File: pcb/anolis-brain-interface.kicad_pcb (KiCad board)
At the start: 2 copper layers, 26 x 26 mm, 12 parts, among them U1 RHD2216, U2 Setebos-I, U3 47571-0001, U4 TPS610994YFF

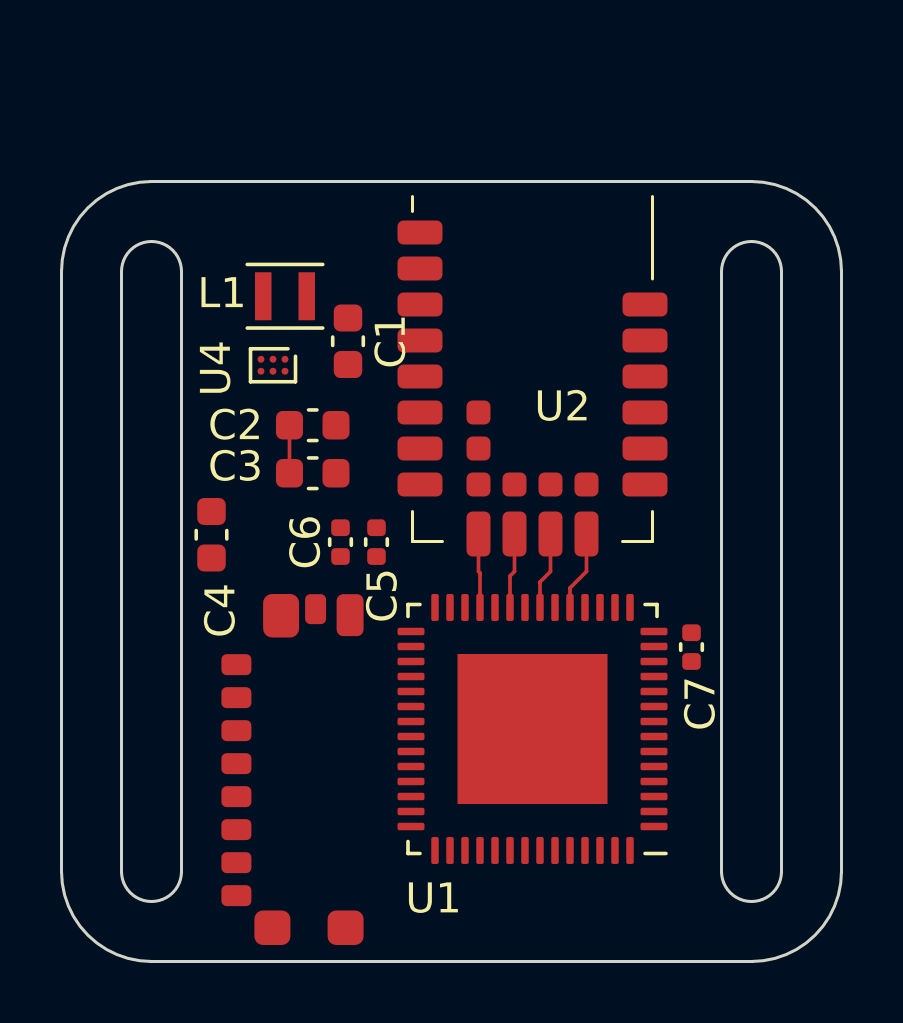
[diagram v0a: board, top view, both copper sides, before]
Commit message: Added battery connector.
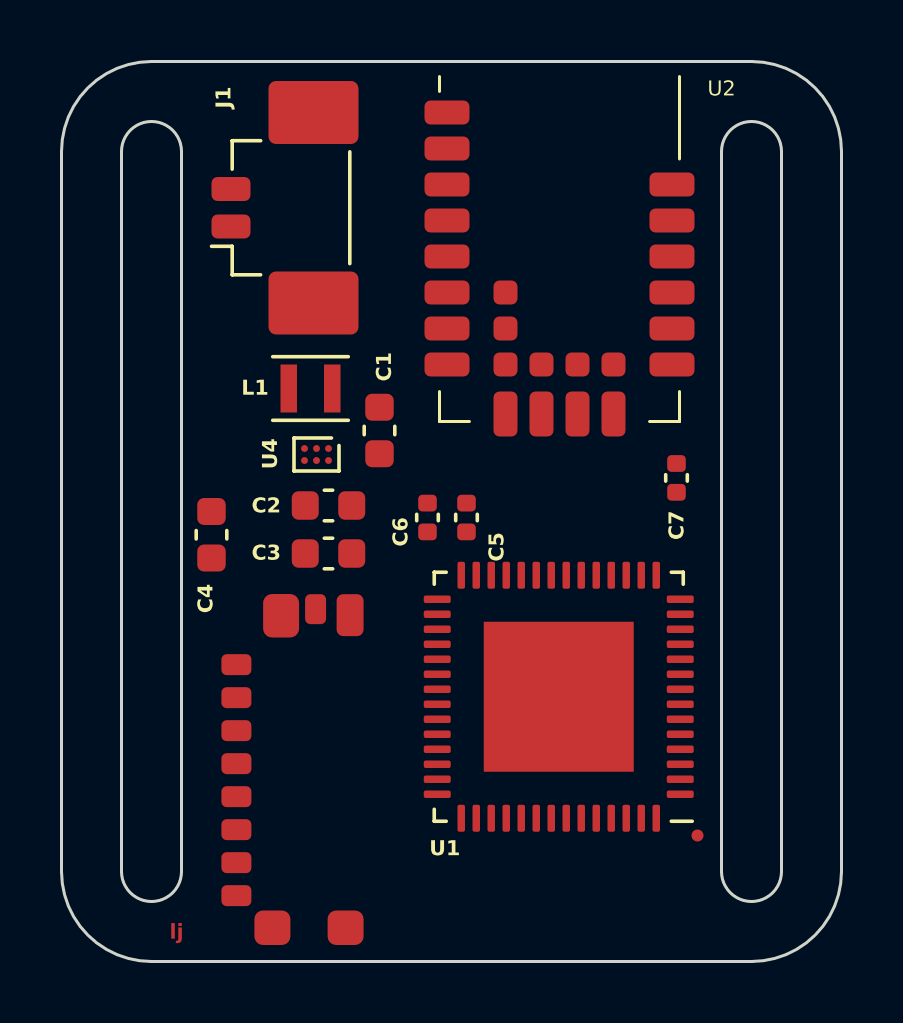
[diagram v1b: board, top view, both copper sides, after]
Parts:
- added J1: 53398-4002, Connector_Molex:Molex_PicoBlade_53398-0271_1x02-1MP_P1.25mm_Vertical, F.Cu at (132.9, 80.9)
- moved C7 5.66 mm to (146.5, 89.9)
- moved U2 4.10 mm to (142.6, 82.0)
- moved U4 3.31 mm to (134.5, 89.1)
- moved L1 3.19 mm to (134.3, 86.9)
- moved C1 3.15 mm to (136.6, 88.3)
- moved C5 3.11 mm to (139.5, 91.2)
- moved C6 3.01 mm to (138.2, 91.2)
- moved C3 2.73 mm to (134.9, 92.4)
- moved C2 2.73 mm to (134.9, 90.8)
- moved U1 1.39 mm to (142.6, 97.2)
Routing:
- net /RHD_~{CS}: track 2.68 -> 0.00 mm
- net /RHD_SCLK: track 2.59 -> 0.00 mm
- net /RHD_MOSI: track 2.51 -> 0.00 mm
- net /RHD_MISO: track 2.47 -> 0.00 mm
- net /VDD: track 1.60 -> 0.00 mm
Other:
- board size 26 x 26 mm -> 26 x 30 mm
- rule pad_to_mask_clearance: 0 -> 0.2
- board text added: "lj"

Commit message: Diode added.
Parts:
- added D1: PMEG2010EJ, Diode_SMD:D_SOD-323F, F.Cu at (131.4, 87.6)
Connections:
- J1 pad 1: /VIN -> Net-(D1-A)
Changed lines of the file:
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@@
   (net 68 "Net-(U4-SW)")
   (net 69 "Net-(U1-ADC_REF)")
+  (net 70 "Net-(D1-A)")
   (footprint "Capacitor_SMD:C_0603_1608Metric" (layer "F.Cu")
     (at 136.6 88.3 -90)
@@
       (stroke (width 0.1) (type solid)) (layer "F.Fab"))
     (pad "1" smd roundrect (at -0.625 -1.25 90) (size 0.8 1.3) (layers "F.Cu" "F.Paste" "F.Mask") (roundrect_rratio 0.25)
-      (net 67 "/VIN") (pinfunction "Pin_1") (pintype "passive"))
+      (net 70 "Net-(D1-A)") (pinfunction "Pin_1") (pintype "passive"))
     (pad "2" smd roundrect (at 0.625 -1.25 90) (size 0.8 1.3) (layers "F.Cu" "F.Paste" "F.Mask") (roundrect_rratio 0.25)
       (net 52 "/GND") (pinfunction "Pin_2") (pintype "passive"))
@@
       (offset (xyz 0 0 0))
       (scale (xyz 1 1 1))
+      (rotate (xyz 0 0 0))
+    )
+  )
+  (footprint "Diode_SMD:D_SOD-323F" (layer "F.Cu")
+    (at 131.4 87.6 90)
+    (descr "SOD-323F http://www.nxp.com/documents/outline_drawing/SOD323F.pdf")
+    (tags "SOD-323F")
+    (property "Sheetfile" "anolis-brain-interface.kicad_sch")
+    (property "Sheetname" "")
+    (property "ki_description" "20V, 1A very low Vf MEGA Schottky barrier rectifier, SOD-323F")
+    (property "ki_keywords" "forward voltage diode")
+    (attr smd)
+    (fp_text reference "D1" (at -2.2 -0.5 90) (layer "F.SilkS")
+        (effects (font (size 0.5 0.5) (thickness 0.1) bold))
+    )
+    (fp_text value "PMEG2010EJ" (at 0.1 1.9 90) (layer "F.Fab")
+        (effects (font (size 1 1) (thickness 0.15)))
+    )
+    (fp_text user "${REFERENCE}" (at 0 -1.85 90) (layer "F.Fab")
+        (effects (font (size 1 1) (thickness 0.15)))
+    )
+    (fp_line (start -1.61 -0.85) (end -1.61 0.85)
+      (stroke (width 0.12) (type solid)) (layer "F.SilkS"))
+    (fp_line (start -1.61 -0.85) (end 1.05 -0.85)
+      (stroke (width 0.12) (type solid)) (layer "F.SilkS"))
+    (fp_line (start -1.61 0.85) (end 1.05 0.85)
+      (stroke (width 0.12) (type solid)) (layer "F.SilkS"))
+    (fp_line (start -1.6 -0.95) (end -1.6 0.95)
+      (stroke (width 0.05) (type solid)) (layer "F.CrtYd"))
+    (fp_line (start -1.6 -0.95) (end 1.6 -0.95)
+      (stroke (width 0.05) (type solid)) (layer "F.CrtYd"))
+    (fp_line (start -1.6 0.95) (end 1.6 0.95)
+      (stroke (width 0.05) (type solid)) (layer "F.CrtYd"))
+    (fp_line (start 1.6 -0.95) (end 1.6 0.95)
+      (stroke (width 0.05) (type solid)) (layer "F.CrtYd"))
+    (fp_line (start -0.9 -0.7) (end 0.9 -0.7)
+      (stroke (width 0.1) (type solid)) (layer "F.Fab"))
+    (fp_line (start -0.9 0.7) (end -0.9 -0.7)
+      (stroke (width 0.1) (type solid)) (layer "F.Fab"))
+    (fp_line (start -0.3 -0.35) (end -0.3 0.35)
+      (stroke (width 0.1) (type solid)) (layer "F.Fab"))
+    (fp_line (start -0.3 0) (end -0.5 0)
+      (stroke (width 0.1) (type solid)) (layer "F.Fab"))
+    (fp_line (start -0.3 0) (end 0.2 -0.35)
+      (stroke (width 0.1) (type solid)) (layer "F.Fab"))
+    (fp_line (start 0.2 -0.35) (end 0.2 0.35)
+      (stroke (width 0.1) (type solid)) (layer "F.Fab"))
+    (fp_line (start 0.2 0) (end 0.45 0)
+      (stroke (width 0.1) (type solid)) (layer "F.Fab"))
+    (fp_line (start 0.2 0.35) (end -0.3 0)
+      (stroke (width 0.1) (type solid)) (layer "F.Fab"))
+    (fp_line (start 0.9 -0.7) (end 0.9 0.7)
+      (stroke (width 0.1) (type solid)) (layer "F.Fab"))
+    (fp_line (start 0.9 0.7) (end -0.9 0.7)
+      (stroke (width 0.1) (type solid)) (layer "F.Fab"))
+    (pad "1" smd roundrect (at -1.1 0 90) (size 0.5 0.5) (layers "F.Cu" "F.Paste" "F.Mask") (roundrect_rratio 0.25)
+      (net 67 "/VIN") (pinfunction "K") (pintype "passive"))
+    (pad "2" smd roundrect (at 1.1 0 90) (size 0.5 0.5) (layers "F.Cu" "F.Paste" "F.Mask") (roundrect_rratio 0.25)
+      (net 70 "Net-(D1-A)") (pinfunction "A") (pintype "passive"))
+    (model "${KICAD6_3DMODEL_DIR}/Diode_SMD.3dshapes/D_SOD-323F.wrl"
+      (offset (xyz 0 0 0))
+      (scale (xyz 1 1 1))

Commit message: Segmented draft.
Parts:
- removed U3: 47571-0001, sd:475710001
- added BT1: Battery_Cell, Battery:BatteryHolder_Keystone_3000_1x12mm, F.Cu at (256.5, 78.7)
- moved C5 11.8 mm to (128.5, 95.5), turned to 180 degrees
- moved C3 11.6 mm to (135.5, 80.8)
- moved C6 11.6 mm to (128.5, 97.5)
- moved C2 11.5 mm to (135.5, 79.3)
- moved C1 11.1 mm to (129.2, 80.0), turned to 90 degrees
- moved C7 9.63 mm to (139.5, 96.5)
- moved U2 9.30 mm to (135.5, 88.0), turned to -90 degrees
- moved U1 9.19 mm to (133.9, 100.1)
- moved U4 8.93 mm to (133.0, 80.3), turned to 0 degrees
- moved D1 8.72 mm to (127.5, 79.8)
- moved C4 8.04 mm to (127.8, 84.4)
- moved L1 7.65 mm to (131.0, 80.0), turned to -90 degrees
- moved J1 6.11 mm to (133.9, 74.8), turned to 180 degrees
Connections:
- U2 pad 10: /RHD_MOSI -> unconnected-(U2-P0.22-Pad10)
- U2 pad 11: /RHD_SCLK -> unconnected-(U2-P0.00/XL1-Pad11)
- U2 pad 12: /RHD_~{CS} -> unconnected-(U2-P0.01/XL2-Pad12)
- U2 pad 13: /SD_DET -> unconnected-(U2-P1.08-Pad13)
- U2 pad 14: /SD_MISO -> /RHD_MISO
- U2 pad 15: /SD_SCLK -> /RHD_MOSI
- U2 pad 16: /SD_MOSI -> /RHD_SCLK
- U2 pad 17: /SD_~{CS} -> /RHD_~{CS}
- U2 pad 9: /RHD_MISO -> unconnected-(U2-P0.19-Pad9)
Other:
- board size 26 x 30 mm -> 140.5 x 40.1 mm

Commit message: New PCB design.
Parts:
- removed BT1: Battery_Cell, Battery:BatteryHolder_Keystone_3000_1x12mm
- removed C4: 10µF, 16V, Capacitor_SMD:C_0603_1608Metric
- removed D1: PMEG2010EJ, Diode_SMD:D_SOD-323F
- removed L1: VLS201610CX-2R2M-1, 2.2µH, Inductor_SMD:L_Murata_DFE201610P
- removed U4: TPS610994YFF, Package_BGA:Texas_DSBGA-6_0.855x1.255mm_Layout2x3_P0.4mm_LevelC
- added TP1: TestPoint, TestPoint:TestPoint_Pad_1.0x1.0mm, F.Cu at (129.0, 98.0)
- added TP2: TestPoint, TestPoint:TestPoint_Pad_1.0x1.0mm, B.Cu at (130.0, 98.0)
- added TP3: TestPoint, TestPoint:TestPoint_Pad_1.0x1.0mm, F.Cu at (131.0, 98.0)
- added TP4: TestPoint, TestPoint:TestPoint_Pad_1.0x1.0mm, B.Cu at (132.0, 98.0)
- added TP5: TestPoint, TestPoint:TestPoint_Pad_1.0x1.0mm, B.Cu at (134.0, 98.0)
- added TP6: TestPoint, TestPoint:TestPoint_Pad_1.0x1.0mm, F.Cu at (135.0, 98.0)
- added TP7: TestPoint, TestPoint:TestPoint_Pad_1.0x1.0mm, B.Cu at (136.0, 98.0)
- added TP8: TestPoint, TestPoint:TestPoint_Pad_1.0x1.0mm, F.Cu at (137.0, 98.0)
- added TP9: TestPoint, TestPoint:TestPoint_Pad_1.0x1.0mm, F.Cu at (133.0, 98.0)
- added U3: TPS70933, Package_TO_SOT_SMD:SOT-23-5, B.Cu at (133.7, 84.1)
- C1, C2, C3, C5, C6, C7, U1: moved to B.Cu
- J1: footprint Connector_Molex:Molex_PicoBlade_53398-0271_1x02-1MP_P1.25mm_Vertical -> zero-hachi:214721-0020
- moved C7 14.8 mm to (127.3, 88.1)
- moved C5 12.9 mm to (138.3, 87.1), turned to 0 degrees
- moved C6 12.9 mm to (138.3, 89.1)
- moved U1 9.54 mm to (132.9, 90.6), turned to 0 degrees
- moved C1 8.35 mm to (136.5, 84.1)
- moved J1 7.82 mm to (132.8, 82.6)
- moved C2 6.70 mm to (130.2, 83.4), turned to 180 degrees
- moved C3 6.70 mm to (130.2, 84.9), turned to 180 degrees
- moved U2 3.09 mm to (134.0, 90.7)
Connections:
- J1 pad 1: Net-(D1-A) -> /VIN
- U1 pad 1: unconnected-(U1-IN4+-Pad1) -> Net-(U1-IN4+)
- U1 pad 2: unconnected-(U1-IN3--Pad2) -> Net-(U1-IN0+)
- U1 pad 3: unconnected-(U1-IN3+-Pad3) -> Net-(U1-IN0+)
- U1 pad 34: unconnected-(U1-IN15--Pad34) -> Net-(U1-IN0+)
- U1 pad 35: unconnected-(U1-IN15+-Pad35) -> Net-(U1-IN0+)
- U1 pad 36: unconnected-(U1-IN14--Pad36) -> Net-(U1-IN0+)
- U1 pad 37: unconnected-(U1-IN14+-Pad37) -> Net-(U1-IN0+)
- U1 pad 38: unconnected-(U1-IN13--Pad38) -> Net-(U1-IN0+)
- U1 pad 39: unconnected-(U1-IN13+-Pad39) -> Net-(U1-IN0+)
- U1 pad 4: unconnected-(U1-IN2--Pad4) -> Net-(U1-IN0+)
- U1 pad 40: unconnected-(U1-IN12--Pad40) -> Net-(U1-IN0+)
- U1 pad 41: unconnected-(U1-IN12+-Pad41) -> Net-(U1-IN0+)
- U1 pad 42: unconnected-(U1-IN11--Pad42) -> Net-(U1-IN0+)
- U1 pad 43: unconnected-(U1-IN11+-Pad43) -> Net-(U1-IN11+)
- U1 pad 44: unconnected-(U1-IN10--Pad44) -> Net-(U1-IN0+)
- U1 pad 45: unconnected-(U1-IN10+-Pad45) -> Net-(U1-IN10+)
- U1 pad 46: unconnected-(U1-IN9--Pad46) -> Net-(U1-IN0+)
- U1 pad 47: unconnected-(U1-IN9+-Pad47) -> Net-(U1-IN9+)
- U1 pad 48: unconnected-(U1-IN8--Pad48) -> Net-(U1-IN0+)
- U1 pad 49: unconnected-(U1-IN8+-Pad49) -> Net-(U1-IN8+)
- U1 pad 5: unconnected-(U1-IN2+-Pad5) -> Net-(U1-IN0+)
- U1 pad 50: unconnected-(U1-IN7--Pad50) -> Net-(U1-IN0+)
- U1 pad 51: unconnected-(U1-IN7+-Pad51) -> Net-(U1-IN7+)
- U1 pad 52: unconnected-(U1-IN6--Pad52) -> Net-(U1-IN0+)
- U1 pad 53: unconnected-(U1-IN6+-Pad53) -> Net-(U1-IN6+)
- U1 pad 54: unconnected-(U1-IN5--Pad54) -> Net-(U1-IN0+)
- U1 pad 55: unconnected-(U1-IN5+-Pad55) -> Net-(U1-IN5+)
- U1 pad 56: unconnected-(U1-IN4--Pad56) -> Net-(U1-IN0+)
- U1 pad 6: unconnected-(U1-IN1--Pad6) -> Net-(U1-IN0+)
- U1 pad 7: unconnected-(U1-IN1+-Pad7) -> Net-(U1-IN0+)
- U1 pad 8: unconnected-(U1-IN0--Pad8) -> Net-(U1-IN0+)
- U1 pad 9: unconnected-(U1-IN0+-Pad9) -> Net-(U1-IN0+)
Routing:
- net Net-(U1-IN4+): track 0.00 -> 4.17 mm, vias 0 -> 1
- net Net-(U1-IN8+): track 0.00 -> 3.66 mm
- net Net-(U1-IN9+): track 0.00 -> 3.66 mm, vias 0 -> 1
- net Net-(U1-IN0+): track 0.00 -> 3.45 mm, vias 0 -> 1
- net Net-(U1-IN7+): track 0.00 -> 3.41 mm
- net Net-(U1-IN5+): track 0.00 -> 3.41 mm
- net Net-(U1-IN6+): track 0.00 -> 3.41 mm, vias 0 -> 1
- net Net-(U1-IN10+): track 0.00 -> 1.21 mm
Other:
- board size 140.5 x 40.1 mm -> 14 x 17 mm

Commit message: PCB done.
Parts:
- added BAT+1: TestPoint, TestPoint:TestPoint_Pad_1.0x1.0mm, F.Cu at (138.2, 82.5)
- added BAT-1: TestPoint, TestPoint:TestPoint_Pad_1.0x1.0mm, F.Cu at (138.2, 84.5)
- added D1: BAT54CW, Package_TO_SOT_SMD:SOT-323_SC-70, B.Cu at (134.1, 83.3)
- added D2: LED, LED_SMD:LED_0402_1005Metric, F.Cu at (126.7, 95.5)
- added R1: 50k, Resistor_SMD:R_0402_1005Metric, B.Cu at (139.4, 83.6)
- added R2: 1k, Resistor_SMD:R_0402_1005Metric, F.Cu at (126.7, 93.5)
- added SW1: EVQ-P7A01P, Button_Switch_SMD:SW_SPST_EVQP7A, F.Cu at (134.3, 82.7)
- added U4: LTC4054ES5-4.2, Package_TO_SOT_SMD:TSOT-23-5, B.Cu at (137.2, 83.6)
- J1: value 53398-4002 -> 214721-0020
- U2: footprint setebos:setebos -> setebos:setebos-no-drc
- U3: footprint Package_TO_SOT_SMD:SOT-23-5 -> Package_TO_SOT_SMD:TSOT-23-5
- moved U3 5.79 mm to (127.9, 83.8), turned to -90 degrees
- moved C1 4.57 mm to (132.0, 83.2), turned to -90 degrees
- moved C3 4.32 mm to (127.1, 87.9), turned to 90 degrees
- moved J1 3.87 mm to (129.1, 81.8)
- moved C7 2.78 mm to (127.4, 90.9)
- moved C6 2.25 mm to (139.3, 87.1), turned to -90 degrees
- moved U2 0.50 mm to (134.0, 91.2)
- moved C2 0.28 mm to (130.4, 83.2), turned to -90 degrees
- moved C5 0.13 mm to (138.2, 87.1), turned to -90 degrees
- renumbered TP1 to IN1, TP2 to IN2, TP3 to IN3, TP4 to IN4, TP5 to IN5, TP6 to IN6, TP7 to IN7, TP8 to IN8, TP9 to REF1
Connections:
- C1 pad 1: /VIN -> /5V
- C2 pad 1: /VDD -> /VIN
- J1 pad 1: /VIN -> /5V
- U2 pad 10: unconnected-(U2-P0.22-Pad10) -> /RHD_MOSI
- U2 pad 11: unconnected-(U2-P0.00/XL1-Pad11) -> /RHD_MISO
- U2 pad 12: unconnected-(U2-P0.01/XL2-Pad12) -> /RHD_~{CS}
- U2 pad 13: unconnected-(U2-P1.08-Pad13) -> Net-(D2-A)
- U2 pad 14: /RHD_MISO -> unconnected-(U2-P1.09-Pad14)
- U2 pad 15: /RHD_MOSI -> unconnected-(U2-P0.11-Pad15)
- U2 pad 16: /RHD_SCLK -> unconnected-(U2-P0.12-Pad16)
- U2 pad 17: /RHD_~{CS} -> unconnected-(U2-P0.03-Pad17)
- U2 pad 7: unconnected-(U2-P0.02-Pad7) -> /~{CHRG}
- U2 pad 9: unconnected-(U2-P0.19-Pad9) -> /RHD_SCLK
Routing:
- net /GND: track 0.00 -> 62.7 mm, vias 0 -> 5
- net Net-(U1-IN0+): track 3.45 -> 41.3 mm
- net /VDD: track 0.00 -> 25.9 mm, vias 0 -> 1
- net /RHD_MISO: track 0.00 -> 15.4 mm, vias 0 -> 1
- net /RHD_MOSI: track 0.00 -> 12.5 mm, vias 0 -> 1
- net /5V: track 0.00 -> 11.5 mm, vias 0 -> 1
- net /RHD_~{CS}: track 0.00 -> 10.8 mm, vias 0 -> 1
- net /~{CHRG}: track 0.00 -> 10.4 mm, vias 0 -> 1
- net /VIN: track 0.00 -> 9.77 mm
- net Net-(SW1-B): track 0.00 -> 9.20 mm, vias 0 -> 1
- net /RHD_SCLK: track 0.00 -> 8.24 mm, vias 0 -> 1
- net Net-(SW1-A): track 0.00 -> 5.24 mm, vias 0 -> 1
- net Net-(U1-IN11+): track 0.00 -> 3.66 mm, vias 0 -> 1
- net Net-(D2-A): track 0.00 -> 3.63 mm
- net Net-(U1-IN10+): track 1.21 -> 3.66 mm
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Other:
- board size 14 x 17 mm -> 14 x 18 mm
- rule pad_to_mask_clearance: 0.2 -> 0.1
- rule solder_mask_min_width: 0.35 -> 0.2
- board text added: "+"
- board text added: "-"
- board text added: "1"
- board text added: "2"
- board text added: "7"
- board text added: "8"
- board text added: "R"

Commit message: Improved routing.
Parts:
- moved R1 0.26 mm to (139.3, 83.8)
- turned C6 to 90 degrees
- turned C5 to 90 degrees
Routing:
- net /GND: track 62.7 -> 63.6 mm

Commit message: PCB version 0.1.0.
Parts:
- renumbered C7 to C4
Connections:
- C2 pad 1: /VIN -> Net-(U3-IN)
- D1 pad 3: /VIN -> Net-(U3-IN)
- U3 pad 1: /VIN -> Net-(U3-IN)
- U3 pad 3: /VIN -> unconnected-(U3-EN-Pad3)
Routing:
- net /VIN: track 9.77 -> 0.00 mm
- net (no net): track 0.00 -> 9.77 mm
